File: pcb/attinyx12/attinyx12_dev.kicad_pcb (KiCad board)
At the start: 2 copper layers, 22.6 x 51 mm, 28 parts, among them J1 USB_C_Receptacle_USB2.0_16P, J2 Conn_01x04, J3 Conn_01x04, J4 Conn_02x06, J5 Conn_01x02, J6 Conn_01x02, U1 USBLC6-2SC6, U2 ATtiny212-SS, U3 CH342K

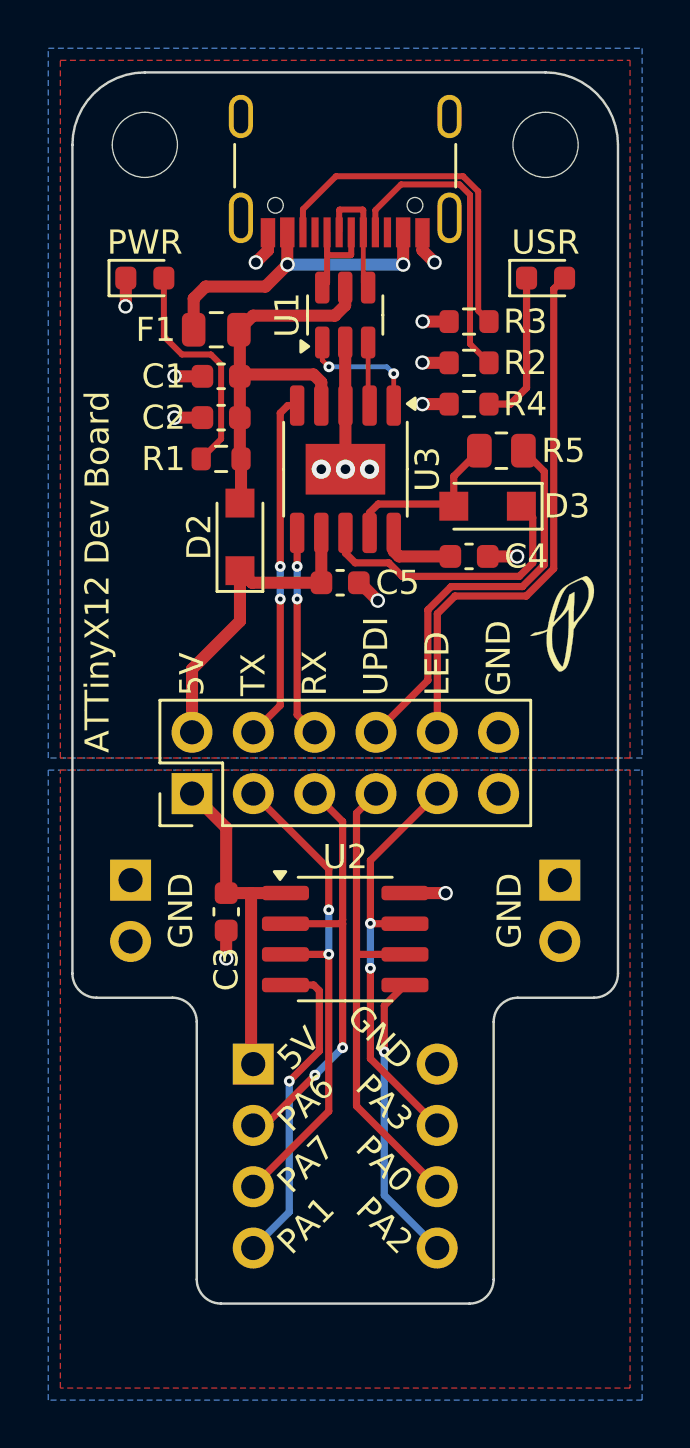
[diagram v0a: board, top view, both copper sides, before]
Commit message: adjustments after DFM analysis
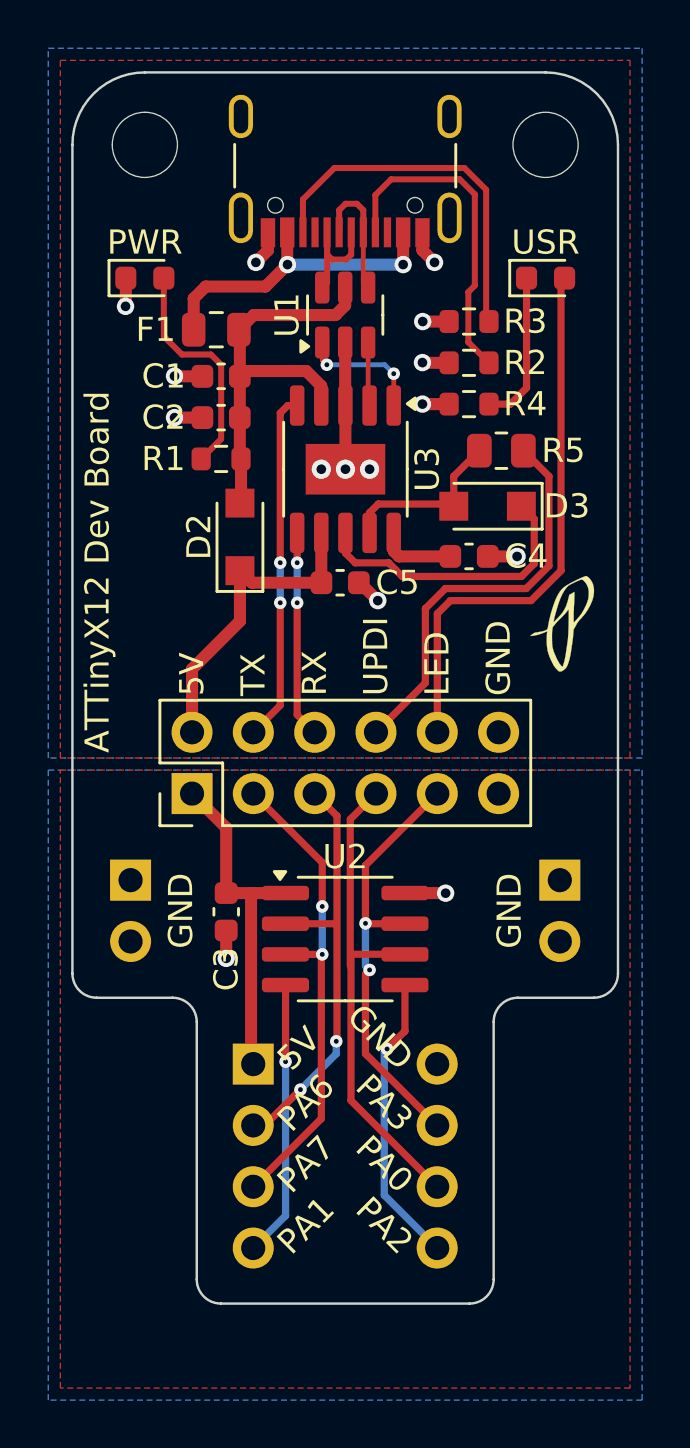
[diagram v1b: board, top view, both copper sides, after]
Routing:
- net /PA1: track 13.3 -> 11.4 mm
- net /PA6: track 18.4 -> 17.5 mm
- net /PA0: track 20.0 -> 20.9 mm
- net Net-(J1-CC1): track 12.7 -> 13.6 mm
- net Net-(J1-CC2): track 14.6 -> 15.2 mm
- net /PA3: track 17.5 -> 18.0 mm
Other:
- outline, holes or cut-outs redrawn
